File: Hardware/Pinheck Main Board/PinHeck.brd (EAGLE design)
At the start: 359.2 x 152.3 mm, 393 parts, among them IC2 PIC32MX795F512L-80I/PT, IC3 CD74HCT244E, IC4 CD74HCT244E, IC5 ULN2803A, J1 N/A, U1 P8X32A-Q44, U10 74HCT2G04GV,125, U11 74HC165D-Q100,118, U12 74HC165D-Q100,118, U13 CAT24M01LI-G, U14 MC74HC08ADR2G, U15 MC74HC08ADR2G, U16 MC74HC08ADR2G, U17 MC74HC08ADR2G, U18 MC74HC08ADR2G, U19 MC74HC08ADR2G, U2 DS1340Z-33+, U20 TIP107, U21 TIP107, U22 TIP107, U23 TIP107, U24 TIP107, U25 TIP107, U26 TIP107, U27 TIP107, U28 TIP102, U29 TIP102, U3 CD74HC595M96, U30 TIP102, U31 TIP102, U32 TIP102, U33 TIP102, U34 TIP102, U35 TIP102, U36 WS2801, U38 WS2801, U39 NCP1117DT33G, U4 CAT24M01LI-G, U5 CD74HC595M96, U52 CD74HC123M96, U6 TPS259251, U7 TPS259261, X1 FQ7050B-8.000, X2 9C-6.500MAAJ-T, X3 ABS25-32.768KHz-1-T

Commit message: Layout done. Silkscreen and TP to do!
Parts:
- removed J12: (no value), PP_Connectors:11216-060_CARDEDGE
- added C38, C42, C62, C63, C64, C65: .1uF, PP_Passives:0805
- moved C53 87.8 mm to (250.4, 134.5)
- moved C29 87.8 mm to (256.9, 132.7)
- moved C50 87.8 mm to (239.2, 132.7)
- moved C52 87.8 mm to (247.8, 134.5)
- moved C51 87.8 mm to (244.7, 134.0)
- moved DMD_PWR 87.8 mm to (250.6, 145.8)
- moved DMD_CON 45.0 mm to (222.6, 145.7)
- moved R34 14.0 mm to (335.5, 137.4), turned to 90 degrees
- moved AUDIO 13.0 mm to (329.7, 152.1)
- moved R32 12.0 mm to (324.1, 137.4), turned to 90 degrees
- moved C28 8.19 mm to (203.5, 132.3), turned to 180 degrees
- moved C24 8.19 mm to (217.2, 132.3), turned to 180 degrees
- moved R152 3.94 mm to (346.5, 114.4)
- moved R156 3.94 mm to (346.5, 130.2)
- moved R45 3.94 mm to (341.1, 127.6)
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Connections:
- removed net N$100: J12.P$88
- removed net N$101: J12.P$89
- removed net N$102: J12.P$90
- removed net N$103: J12.P$101
- removed net N$104: J12.P$103
- removed net N$105: J12.P$105
- removed net N$106: J12.P$107
- removed net N$107: J12.P$109
- removed net N$108: J12.P$111
- removed net N$109: J12.P$113
- removed net N$110: J12.P$115
- removed net N$111: J12.P$117
- removed net N$112: J12.P$119
- removed net N$133: J12.P$18
- removed net N$134: J12.P$20
- removed net N$135: J12.P$22
- removed net N$136: J12.P$24
- removed net N$137: J12.P$26
- removed net N$138: J12.P$28
- removed net N$139: J12.P$30
- removed net N$140: J12.P$32
- removed net N$141: J12.P$34
- removed net N$142: J12.P$36
- removed net N$143: J12.P$38
- removed net N$144: J12.P$40
- removed net N$145: J12.P$60
- removed net N$146: J12.P$59
- removed net N$147: J12.P$58
- removed net N$148: J12.P$57
- removed net N$149: J12.P$56
- removed net N$150: J12.P$55
- removed net N$151: J12.P$54
- removed net N$152: J12.P$53
- removed net N$153: J12.P$52
- removed net N$154: J12.P$51
- removed net N$155: J12.P$62
- removed net N$156: J12.P$64
- removed net N$157: J12.P$66
- removed net N$158: J12.P$68
- removed net N$159: J12.P$70
- removed net N$160: J12.P$72
- removed net N$161: J12.P$74
- removed net N$162: J12.P$76
- removed net N$163: J12.P$78
- removed net N$164: J12.P$80
- removed net N$165: J12.P$100
- removed net N$166: J12.P$99
- removed net N$167: J12.P$98
- removed net N$168: J12.P$97
- removed net N$169: J12.P$96
- removed net N$170: J12.P$95
- removed net N$171: J12.P$94
- removed net N$172: J12.P$93
- removed net N$173: J12.P$92
- removed net N$174: J12.P$91
- removed net N$175: J12.P$102
- removed net N$176: J12.P$104
- removed net N$177: J12.P$106
- removed net N$178: J12.P$108
- removed net N$179: J12.P$110
- removed net N$180: J12.P$112
- removed net N$181: J12.P$114
- removed net N$182: J12.P$116
- removed net N$183: J12.P$118
- removed net N$184: J12.P$120
- removed net N$62: J12.P$19
- removed net N$63: J12.P$21
- removed net N$64: J12.P$23
- removed net N$65: J12.P$25
- removed net N$66: J12.P$27
- removed net N$67: J12.P$29
- removed net N$68: J12.P$31
- removed net N$69: J12.P$33
- removed net N$70: J12.P$35
- removed net N$71: J12.P$37
- removed net N$72: J12.P$39
- removed net N$73: J12.P$41
- removed net N$74: J12.P$42
- removed net N$75: J12.P$43
- removed net N$76: J12.P$44
- removed net N$77: J12.P$45
- removed net N$78: J12.P$46
- removed net N$79: J12.P$47
- removed net N$80: J12.P$48
- removed net N$81: J12.P$49
- removed net N$82: J12.P$50
- removed net N$83: J12.P$61
- removed net N$84: J12.P$63
- removed net N$85: J12.P$65
- removed net N$86: J12.P$67
- removed net N$87: J12.P$69
- removed net N$88: J12.P$71
- removed net N$89: J12.P$73
- removed net N$90: J12.P$75
- removed net N$91: J12.P$77
- removed net N$92: J12.P$79
- removed net N$93: J12.P$81
- removed net N$94: J12.P$82
- removed net N$95: J12.P$83
- removed net N$96: J12.P$84
- removed net N$97: J12.P$85
- removed net N$98: J12.P$86
- removed net N$99: J12.P$87
- net 5V: now also C38.1, C42.1, C62.1, C63.1, C64.1, C65.1
- net AUD0: no longer J12.P$5
- net AUD1: no longer J12.P$6
- net BACK_OUT: no longer J12.P$11
- net COIN_OUT: no longer J12.P$13
- net DOOR_OUT: no longer J12.P$10
- net ENTER_OUT: no longer J12.P$12
- net GI_R_6: no longer J12.P$17
- net GI_R_7: no longer J12.P$16
- net GND: now also C38.2, C42.2, C62.2, C63.2, C64.2, C65.2
- net L_FLIP_OUT: no longer J12.P$7
- net R_FLIP_OUT: no longer J12.P$8
- net SD_CS: no longer J12.P$1
- net SD_DI: no longer J12.P$2
- net SD_DO: no longer J12.P$4
- net SD_SCLK: no longer J12.P$3
- net ST_BU_OUT: no longer J12.P$15
- net TILT_OUT: no longer J12.P$14
- net USER_0_OUT: no longer J12.P$9
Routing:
- net GI_R_6: track 204.1 -> 22.4 mm, vias 1 -> 0
- net GI_R_7: track 197.6 -> 24.8 mm, vias 1 -> 0
- net ST_BU_OUT: track 149.3 -> 6.85 mm, vias 1 -> 0
- net TILT_OUT: track 143.9 -> 6.80 mm, vias 1 -> 0
- net COIN_OUT: track 140.9 -> 6.76 mm, vias 1 -> 0
- net USER_0_OUT: track 139.9 -> 6.80 mm, vias 1 -> 0
- net L_FLIP_OUT: track 139.3 -> 6.82 mm, vias 1 -> 0
- net R_FLIP_OUT: track 138.8 -> 6.75 mm, vias 1 -> 0
- net DOOR_OUT: track 138.4 -> 6.74 mm, vias 1 -> 0
- net BACK_OUT: track 137.9 -> 6.78 mm, vias 1 -> 0
- net ENTER_OUT: track 137.2 -> 6.82 mm, vias 1 -> 0
- net AUD0: track 266.2 -> 165.0 mm, vias 2 -> 0
- net AUD1: track 270.3 -> 175.8 mm, vias 2 -> 0
- net SD_DO: track 191.6 -> 132.7 mm, vias 4 -> 2
- net SD_SCLK: track 185.9 -> 130.6 mm, vias 4 -> 2
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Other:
- outline, holes or cut-outs redrawn

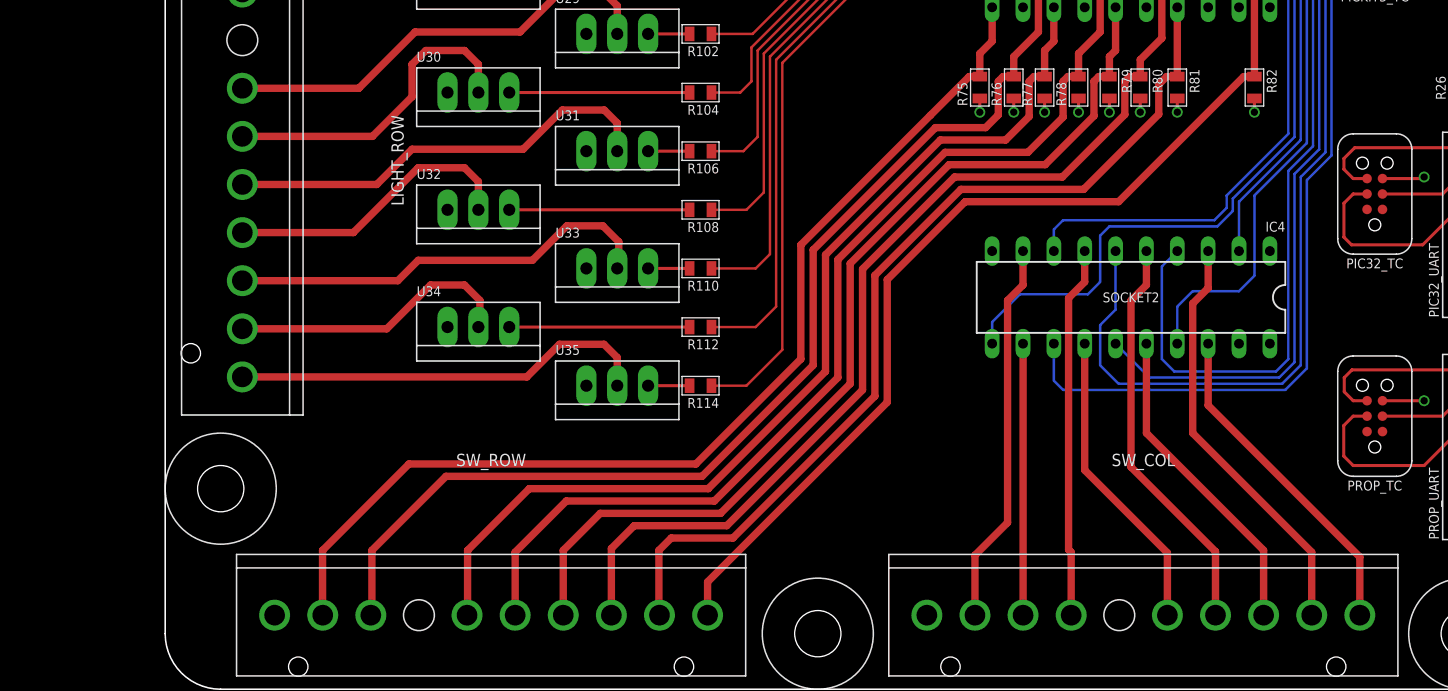
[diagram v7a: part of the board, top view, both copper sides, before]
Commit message: Started Test Points
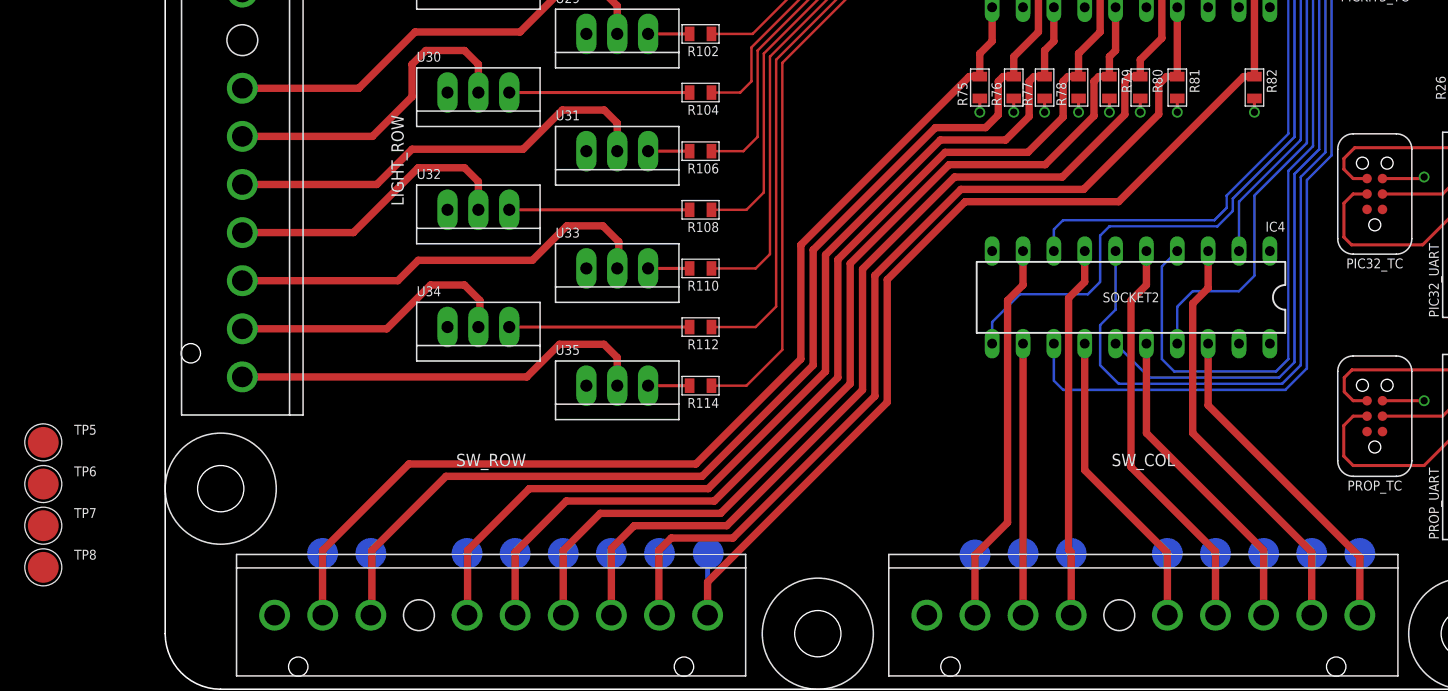
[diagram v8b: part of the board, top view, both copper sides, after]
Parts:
- added SW_C_0, SW_C_1, SW_C_2, SW_C_3, SW_C_4, SW_C_5, SW_C_6, SW_C_7, SW_R_0, SW_R_1, SW_R_2, SW_R_3, SW_R_4, SW_R_5, SW_R_6, SW_R_7, TP5, TP6, TP7, TP8: (no value), PP_Connectors:100MIL_TP
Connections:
- new net N$16: TP5.P$1, TP6.P$1, TP7.P$1, TP8.P$1
- net SW_C_0: now also SW_C_0.P$1
- net SW_C_1: now also SW_C_1.P$1
- net SW_C_2: now also SW_C_2.P$1
- net SW_C_3: now also SW_C_3.P$1
- net SW_C_4: now also SW_C_4.P$1
- net SW_C_5: now also SW_C_5.P$1
- net SW_C_6: now also SW_C_6.P$1
- net SW_C_7: now also SW_C_7.P$1
- net SW_R_0: now also SW_R_0.P$1
- net SW_R_1: now also SW_R_1.P$1
- net SW_R_2: now also SW_R_2.P$1
- net SW_R_3: now also SW_R_3.P$1
- net SW_R_4: now also SW_R_4.P$1
- net SW_R_5: now also SW_R_5.P$1
- net SW_R_6: now also SW_R_6.P$1
- net SW_R_7: now also SW_R_7.P$1
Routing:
- net SW_R_0: track 84.8 -> 90.0 mm
- net SW_R_7: track 87.2 -> 92.3 mm
- net SW_R_3: track 79.8 -> 84.9 mm
- net SW_C_5: track 30.6 -> 35.7 mm
- net SW_C_0: track 27.5 -> 32.6 mm
- net SW_R_6: track 96.2 -> 101.3 mm
- net SW_R_5: track 82.3 -> 87.4 mm
- net SW_R_4: track 89.8 -> 94.9 mm
- net SW_R_2: track 87.1 -> 92.2 mm
- net SW_R_1: track 77.1 -> 82.2 mm
- net SW_C_6: track 22.4 -> 27.4 mm
- net SW_C_4: track 25.2 -> 30.3 mm
- net SW_C_3: track 33.4 -> 38.5 mm
- net SW_C_2: track 26.3 -> 31.4 mm
- net SW_C_1: track 34.6 -> 39.6 mm
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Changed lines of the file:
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@@
 <?xml version="1.0" encoding="utf-8"?>
 <!DOCTYPE eagle SYSTEM "eagle.dtd">
-<eagle version="6.6.0">
+<eagle version="6.5.0">
 <drawing>
 <settings>
@@
 <element name="C64" library="PP_Passives" package="0805" value=".1uF" x="234.442" y="57.15"/>
 <element name="C65" library="PP_Passives" package="0805" value=".1uF" x="253.746" y="57.15"/>
+<element name="SW_R_7" library="PP_Connectors" package="100MIL_TP" value="" x="12.954" y="11.176" rot="MR90"/>
+<element name="SW_R_6" library="PP_Connectors" package="100MIL_TP" value="" x="16.92875" y="11.176" rot="MR90"/>
+<element name="SW_R_5" library="PP_Connectors" package="100MIL_TP" value="" x="24.84875" y="11.176" rot="MR90"/>
+<element name="SW_R_4" library="PP_Connectors" package="100MIL_TP" value="" x="28.80875" y="11.176" rot="MR90"/>
+<element name="SW_R_3" library="PP_Connectors" package="100MIL_TP" value="" x="32.766" y="11.176" rot="MR90"/>
+<element name="SW_R_2" library="PP_Connectors" package="100MIL_TP" value="" x="36.72875" y="11.176" rot="MR90"/>
+<element name="SW_R_1" library="PP_Connectors" package="100MIL_TP" value="" x="40.68875" y="11.176" rot="MR90"/>
+<element name="SW_R_0" library="PP_Connectors" package="100MIL_TP" value="" x="44.704" y="11.176" rot="MR90"/>
+<element name="SW_C_7" library="PP_Connectors" package="100MIL_TP" value="" x="66.658" y="11.049" rot="MR90"/>
+<element name="SW_C_6" library="PP_Connectors" package="100MIL_TP" value="" x="70.618" y="11.176" rot="MR90"/>
+<element name="SW_C_5" library="PP_Connectors" package="100MIL_TP" value="" x="74.578" y="11.176" rot="MR90"/>
+<element name="SW_C_4" library="PP_Connectors" package="100MIL_TP" value="" x="82.498" y="11.176" rot="MR90"/>
+<element name="SW_C_3" library="PP_Connectors" package="100MIL_TP" value="" x="86.458" y="11.176" rot="MR90"/>
+<element name="SW_C_2" library="PP_Connectors" package="100MIL_TP" value="" x="90.418" y="11.176" rot="MR90"/>
+<element name="SW_C_1" library="PP_Connectors" package="100MIL_TP" value="" x="94.378" y="11.176" rot="MR90"/>
+<element name="SW_C_0" library="PP_Connectors" package="100MIL_TP" value="" x="98.338" y="11.176" rot="MR90"/>
+<element name="TP5" library="PP_Connectors" package="100MIL_TP" value="" x="-10.033" y="20.32"/>
+<element name="TP6" library="PP_Connectors" package="100MIL_TP" value="" x="-10.033" y="16.891"/>
+<element name="TP7" library="PP_Connectors" package="100MIL_TP" value="" x="-10.033" y="13.462"/>
+<element name="TP8" library="PP_Connectors" package="100MIL_TP" value="" x="-10.033" y="10.033"/>
 </elements>
 <signals>
@@
 <wire x1="71.882" y1="54.102" x2="69.85" y2="52.07" width="0.6096" layer="1"/>
 <wire x1="69.85" y1="52.07" x2="69.85" y2="50.43" width="0.6096" layer="1"/>
+<contactref element="SW_R_6" pad="P$1"/>
+<wire x1="16.92875" y1="11.176" x2="16.92875" y2="6.096" width="0.4064" layer="16"/>
 </signal>
 <signal name="SW_R_5">
@@
 <wire x1="73.152" y1="53.34" x2="72.39" y2="52.578" width="0.6096" layer="1"/>
 <wire x1="72.39" y1="52.578" x2="72.39" y2="50.43" width="0.6096" layer="1"/>
+<contactref element="SW_R_5" pad="P$1"/>
+<wire x1="24.84875" y1="11.176" x2="24.84875" y2="6.096" width="0.4064" layer="16"/>
 </signal>
 <signal name="SW_R_4">
@@
 <wire x1="76.962" y1="54.102" x2="75.184" y2="52.324" width="0.6096" layer="1"/>
 <wire x1="75.184" y1="52.324" x2="75.184" y2="50.43" width="0.6096" layer="1"/>
+<contactref element="SW_R_4" pad="P$1"/>
+<wire x1="28.80875" y1="11.176" x2="28.80875" y2="6.096" width="0.4064" layer="16"/>
 </signal>
 <signal name="SW_R_3">
@@
 <wire x1="32.766" y1="11.43" x2="32.766" y2="6.09875" width="0.6096" layer="1"/>
 <wire x1="32.766" y1="6.09875" x2="32.76875" y2="6.096" width="0.6096" layer="1"/>
+<contactref element="SW_R_3" pad="P$1"/>
+<wire x1="32.766" y1="11.176" x2="32.76875" y2="11.176" width="0.4064" layer="16"/>
+<wire x1="32.76875" y1="11.176" x2="32.76875" y2="6.096" width="0.4064" layer="16"/>
 </signal>
 <signal name="SW_R_1">
@@
 <wire x1="40.64" y1="11.43" x2="40.64" y2="6.14475" width="0.6096" layer="1"/>
 <wire x1="40.64" y1="6.14475" x2="40.68875" y2="6.096" width="0.6096" layer="1"/>
+<contactref element="SW_R_1" pad="P$1"/>
+<wire x1="40.68875" y1="11.176" x2="40.68875" y2="6.096" width="0.4064" layer="16"/>
 </signal>
 <signal name="SW_R_0">
@@
 <wire x1="44.704" y1="6.15125" x2="44.64875" y2="6.096" width="0.6096" layer="1"/>
 <wire x1="44.64875" y1="8.83475" x2="44.64875" y2="6.096" width="0.6096" layer="1"/>
+<contactref element="SW_R_0" pad="P$1"/>
+<wire x1="44.704" y1="11.176" x2="44.64875" y2="11.176" width="0.4064" layer="16"/>
+<wire x1="44.64875" y1="11.176" x2="44.64875" y2="6.096" width="0.4064" layer="16"/>
 </signal>
 <signal name="SW_C_7">
@@
 <wire x1="69.342" y1="32.004" x2="70.612" y2="33.274" width="0.6096" layer="1"/>
 <wire x1="70.612" y1="33.274" x2="70.612" y2="36.068" width="0.6096" layer="1"/>
+<contactref element="SW_C_7" pad="P$1"/>
+<wire x1="66.658" y1="11.049" x2="66.658" y2="6.096" width="0.4064" layer="16"/>
 </signal>
 <signal name="SW_C_6">
@@
 <wire x1="70.618" y1="6.096" x2="70.618" y2="28.442" width="0.6096" layer="1"/>
 <wire x1="70.618" y1="28.442" x2="70.612" y2="28.448" width="0.6096" layer="1"/>
+<contactref element="SW_C_6" pad="P$1"/>
+<wire x1="70.618" y1="11.176" x2="70.618" y2="6.096" width="0.4064" layer="16"/>
 </signal>
 <signal name="SW_C_4">
@@
 <wire x1="82.498" y1="11.228" x2="75.692" y2="18.034" width="0.6096" layer="1"/>
 <wire x1="75.692" y1="18.034" x2="75.692" y2="28.448" width="0.6096" layer="1"/>
+<contactref element="SW_C_4" pad="P$1"/>
+<wire x1="82.498" y1="11.176" x2="82.498" y2="6.096" width="0.4064" layer="16"/>
 </signal>
 <signal name="SW_C_5">
@@
 <wire x1="74.364390625" y1="32.200390625" x2="75.692" y2="33.528" width="0.6096" layer="1"/>
 <wire x1="75.692" y1="33.528" x2="75.692" y2="36.068" width="0.6096" layer="1"/>
+<contactref element="SW_C_5" pad="P$1"/>
+<wire x1="74.578" y1="11.176" x2="74.578" y2="6.096" width="0.4064" layer="16"/>
 </signal>
 <signal name="SW_C_3">
@@
 <wire x1="79.502" y1="32.004" x2="80.772" y2="33.274" width="0.6096" layer="1"/>
 <wire x1="80.772" y1="33.274" x2="80.772" y2="36.068" width="0.6096" layer="1"/>
+<contactref element="SW_C_3" pad="P$1"/>
+<wire x1="86.458" y1="11.176" x2="86.458" y2="6.096" width="0.4064" layer="16"/>
 </signal>
 <signal name="SW_C_2">
@@
 <wire x1="90.418" y1="11.436" x2="80.772" y2="21.082" width="0.6096" layer="1"/>
 <wire x1="80.772" y1="21.082" x2="80.772" y2="28.448" width="0.6096" layer="1"/>
+<contactref element="SW_C_2" pad="P$1"/>
+<wire x1="90.418" y1="11.176" x2="90.418" y2="6.096" width="0.4064" layer="16"/>
 </signal>
 <signal name="SW_C_1">
@@
 <wire x1="84.582" y1="31.75" x2="85.852" y2="33.02" width="0.6096" layer="1"/>
 <wire x1="85.852" y1="33.02" x2="85.852" y2="36.068" width="0.6096" layer="1"/>
+<contactref element="SW_C_1" pad="P$1"/>
+<wire x1="94.378" y1="11.176" x2="94.378" y2="6.096" width="0.4064" layer="16"/>
 </signal>
 <signal name="SW_C_0">
@@
 <wire x1="98.338" y1="10.882" x2="85.852" y2="23.368" width="0.6096" layer="1"/>
 <wire x1="85.852" y1="23.368" x2="85.852" y2="28.448" width="0.6096" layer="1"/>
+<contactref element="SW_C_0" pad="P$1"/>
+<wire x1="98.338" y1="11.176" x2="98.338" y2="6.096" width="0.4064" layer="16"/>
 </signal>
 <signal name="SW_R_7">
@@
 <contactref element="SW_ROW" pad="P$2"/>
 <wire x1="67.056" y1="50.43" x2="66.178" y2="50.43" width="0.6096" layer="1"/>
-<wire x1="66.178" y1="50.43" x2="62.992" y2="47.244" width="0.6096" layer="1"/>
-<wire x1="62.992" y1="47.244" x2="52.324" y2="36.576" width="0.6096" layer="1"/>
+<wire x1="66.178" y1="50.43" x2="52.324" y2="36.576" width="0.6096" layer="1"/>
 <wire x1="52.324" y1="36.576" x2="52.324" y2="27.178" width="0.6096" layer="1"/>
 <wire x1="52.324" y1="27.178" x2="43.688" y2="18.542" width="0.6096" layer="1"/>
@@
 <wire x1="68.072" y1="53.34" x2="67.056" y2="52.324" width="0.6096" layer="1"/>
 <wire x1="67.056" y1="52.324" x2="67.056" y2="50.43" width="0.6096" layer="1"/>
+<contactref element="SW_R_7" pad="P$1"/>
+<wire x1="12.954" y1="11.176" x2="12.96875" y2="11.176" width="0.4064" layer="16"/>
+<wire x1="12.96875" y1="11.176" x2="12.96875" y2="6.096" width="0.4064" layer="16"/>
 </signal>
 <signal name="SW_R_2">
@@
 <wire x1="38.608" y1="13.462" x2="36.72875" y2="11.58275" width="0.6096" layer="1"/>
 <wire x1="36.72875" y1="11.58275" x2="36.72875" y2="6.096" width="0.6096" layer="1"/>
+<contactref element="SW_R_2" pad="P$1"/>
+<wire x1="36.72875" y1="11.176" x2="36.72875" y2="6.096" width="0.4064" layer="16"/>
 </signal>
 <signal name="PIC_SW_R_0">
@@
 <wire x1="22.844" y1="130.17" x2="22.844" y2="131.596" width="0.254" layer="1"/>
 </signal>
+<signal name="N$16">
+<contactref element="TP5" pad="P$1"/>
+<contactref element="TP6" pad="P$1"/>
+<contactref element="TP7" pad="P$1"/>
+<contactref element="TP8" pad="P$1"/>
+<wire x1="-10.033" y1="13.462" x2="-10.033" y2="10.033" width="0" layer="19" extent="1-1"/>
+<wire x1="-10.033" y1="16.891" x2="-10.033" y2="13.462" width="0" layer="19" extent="1-1"/>
+<wire x1="-10.033" y1="20.32" x2="-10.033" y2="16.891" width="0" layer="19" extent="1-1"/>
+</signal>
 </signals>
